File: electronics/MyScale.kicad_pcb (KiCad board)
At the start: 4 copper layers, 80 x 60.1 mm, 101 parts, among them J1 Conn_01x03, J10 Conn_02x03_Odd_Even, J2 Conn_01x03, J3 Conn_01x03, J4 Conn_01x03, J5 Conn_01x02_MountingPin, J6 12402012E212A, J7 SIM_Card, J8 Conn_01x02_MountingPin, J9 Conn_Coaxial_Small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

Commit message: electronics: add 3D models
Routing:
- net GND: vias 116 -> 135
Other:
- board size 80 x 60.1 mm -> 80 x 60 mm
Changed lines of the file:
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@@
 		(sheetname "/Charger/")
 		(sheetfile "charger.kicad_sch")
-		(units
-			(unit
-				(name "A")
-				(pins "1" "6" "16" "2" "4" "9" "11" "12" "17" "8" "5" "13" "14" "15"
-					"10" "3" "7"
-				)
-			)
-		)
 		(attr smd)
 		(duplicate_pad_numbers_are_jumpers no)
@@
 		)
 		(embedded_fonts no)
-		(model "../nRobotics.3dshapes/TI_RTE0016C.stp"
+		(model "${KIPRJMOD}/MyScale.3dshapes/TI_RTE0016C.stp"
 			(offset
 				(xyz 0 0 0)
@@
 		(sheetname "/Radio/")
 		(sheetfile "radio.kicad_sch")
-		(units
-			(unit
-				(name "A")
-				(pins "1" "2" "4" "6" "3" "11" "5" "9" "10" "7" "8")
-			)
-		)
 		(attr smd)
 		(duplicate_pad_numbers_are_jumpers no)
@@
 		)
 		(embedded_fonts no)
-		(model "${KIPRJMOD}/portsupply.3dshapes/TI_DQC0010A.stp"
+		(model "${KIPRJMOD}/MyScale.3dshapes/TI_DQC0010A.stp"
 			(offset
 				(xyz 0 0 0)
@@
 	)
 	(gr_line
-		(start 65 114.905)
+		(start 65 115)
 		(end 145 115)
 		(stroke
@@
 	(gr_line
 		(start 65 175)
-		(end 65 114.905)
+		(end 65 115)
 		(stroke
 			(width 0.05)
@@
 	)
 	(via
+		(at 126.3 142.65)
+		(size 0.45)
+		(drill 0.25)
+		(layers "F.Cu" "B.Cu")
+		(free yes)
+		(net "GND")
+	)
+	(via
+		(at 138.7 126.95)
+		(size 0.6)
+		(drill 0.3)
+		(layers "F.Cu" "B.Cu")
+		(free yes)
+		(net "GND")
+	)
+	(via
 		(at 106.45 134.7)
 		(size 0.45)
@@
 	)
 	(via
+		(at 103.15 151.75)
+		(size 0.6)
+		(drill 0.3)
+		(layers "F.Cu" "B.Cu")
+		(free yes)
+		(net "GND")
+	)
+	(via
 		(at 103.75 122.7)
 		(size 0.6)
@@
 	)
 	(via
+		(at 139.75 128.15)
+		(size 0.6)
+		(drill 0.3)
+		(layers "F.Cu" "B.Cu")
+		(free yes)
+		(net "GND")
+	)
+	(via
 		(at 111.2 148.55)
 		(size 0.6)
@@
 	)
 	(via
+		(at 134.75 128.15)
+		(size 0.6)
+		(drill 0.3)
+		(layers "F.Cu" "B.Cu")
+		(free yes)
+		(net "GND")
+	)
+	(via
 		(at 86.45 131.85)
 		(size 0.6)
@@
 	)
 	(via
-		(at 126.5 142.15)
+		(at 126.2 141.85)
 		(size 0.45)
 		(drill 0.25)
@@
 	)
 	(via
+		(at 74.5 143.05)
+		(size 0.45)
+		(drill 0.25)
+		(layers "F.Cu" "B.Cu")
+		(free yes)
+		(net "GND")
+	)
+	(via
 		(at 142.8 160.4)
 		(size 0.6)
@@
 	)
 	(via
+		(at 123.25 141.25)
+		(size 0.6)
+		(drill 0.3)
+		(layers "F.Cu" "B.Cu")
+		(free yes)
+		(net "GND")
+	)
+	(via
 		(at 102 125)
 		(size 0.6)
@@
 	)
 	(via
+		(at 137.1 146.85)
+		(size 0.6)
+		(drill 0.3)
+		(layers "F.Cu" "B.Cu")
+		(free yes)
+		(net "GND")
+	)
+	(via
 		(at 96.6 173.25)
 		(size 0.6)
@@
 	)
 	(via
+		(at 135.5 126.85)
+		(size 0.6)
+		(drill 0.3)
+		(layers "F.Cu" "B.Cu")
+		(free yes)
+		(net "GND")
+	)
+	(via
 		(at 112.7 151.7)
 		(size 0.6)
@@
 	)
 	(via
+		(at 137.15 126.95)
+		(size 0.6)
+		(drill 0.3)
+		(layers "F.Cu" "B.Cu")
+		(free yes)
+		(net "GND")
+	)
+	(via
+		(at 101.95 156.3)
+		(size 0.6)
+		(drill 0.3)
+		(layers "F.Cu" "B.Cu")
+		(free yes)
+		(net "GND")
+	)
+	(via
 		(at 90.4 147.1)
 		(size 0.6)
@@
 	)
 	(via
+		(at 104.45 150.4)
+		(size 0.6)
+		(drill 0.3)
+		(layers "F.Cu" "B.Cu")
+		(free yes)
+		(net "GND")
+	)
+	(via
 		(at 92.3 135.35)
 		(size 0.6)
@@
 	)
 	(via
+		(at 70.3 129.65)
+		(size 0.6)
+		(drill 0.3)
+		(layers "F.Cu" "B.Cu")
+		(free yes)
+		(net "GND")
+	)
+	(via
 		(at 103.85 136.45)
 		(size 0.45)
@@
 	)
 	(via
+		(at 135.35 146.35)
+		(size 0.6)
+		(drill 0.3)
+		(layers "F.Cu" "B.Cu")
+		(free yes)
+		(net "GND")
+	)
+	(via
 		(at 112.1 133.8)
 		(size 0.45)
@@
 	)
 	(via
+		(at 74.45 145.25)
+		(size 0.45)
+		(drill 0.25)
+		(layers "F.Cu" "B.Cu")
+		(free yes)
+		(net "GND")
+	)
+	(via
+		(at 134.1 143.6)
+		(size 0.6)
+		(drill 0.3)
+		(layers "F.Cu" "B.Cu")
+		(free yes)
+		(net "GND")
+	)
+	(via
 		(at 78.25 132.45)
 		(size 0.6)
@@
 	)
 	(via
+		(at 108.5 155.95)
+		(size 0.6)
+		(drill 0.3)
+		(layers "F.Cu" "B.Cu")
+		(free yes)
+		(net "GND")
+	)
+	(via
 		(at 106.85 116.65)
 		(size 0.6)
@@
 	)
 	(via
+		(at 68.85 128.5)
+		(size 0.6)
+		(drill 0.3)
+		(layers "F.Cu" "B.Cu")
+		(free yes)
+		(net "GND")
+	)
+	(via
 		(at 113 146.15)
 		(size 0.45)
@@
 	)
 	(via
+		(at 116.4 164.8)
+		(size 0.6)
+		(drill 0.3)
+		(layers "F.Cu" "B.Cu")
+		(free yes)
+		(net "GND")
+	)
+	(via
 		(at 92.05 142.55)
 		(size 0.6)
@@
 		(polygon
 			(pts
-				(xy 65.05 115) (xy 145 115) (xy 145.05 175.1) (xy 65.05 175.1)
+				(xy 65 115) (xy 145 115) (xy 145 175) (xy 65 175)
 			)
 		)

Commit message: electronics: final touches
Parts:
- removed C3, C7: C, Capacitor_SMD:C_0402_1005Metric
- removed R15: 0R, Resistor_SMD:R_0402_1005Metric
- added Q2: Q_NMOS_GSD, Package_TO_SOT_SMD:SOT-23-3, F.Cu at (107.5, 130.7)
- added R30: 10k, Resistor_SMD:R_0603_1608Metric, F.Cu at (107.5, 127.9)
- added R31: 0R, Resistor_SMD:R_0603_1608Metric, F.Cu at (74.5, 152.2)
- added REF**: Tab, MyScale:KikitTab, F.Cu at (105.6, 114.3)
- added REF**: Tab, MyScale:KikitTab, F.Cu at (110.4, 175.6)
- added REF**: Tab, MyScale:KikitTab, F.Cu at (64.1, 145.9)
- added REF**: Tab, MyScale:KikitTab, F.Cu at (145.7, 147.8)
- added TP1: TestPoint, TestPoint:TestPoint_Pad_D1.0mm, B.Cu at (75.6, 134.2)
- added TP2: TestPoint, TestPoint:TestPoint_Pad_D1.0mm, B.Cu at (85.3, 154.4)
- added TP3: TestPoint, TestPoint:TestPoint_Pad_D1.0mm, B.Cu at (111.3, 146.0)
- added TP4: TestPoint, TestPoint:TestPoint_Pad_D1.0mm, B.Cu at (104.8, 142.9)
- U3: value ~ -> TXU0202
- moved J9 3.82 mm to (88.3, 122.4)
- moved D2 2.40 mm to (104.0, 132.2)
- moved R11 2.40 mm to (104.2, 129.1)
- moved R12 2.40 mm to (104.2, 130.6)
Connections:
- J7 pad CD: (no net) -> /Radio/SimDet
- J7 pad SH: (no net) -> GND
- J9 pad 1: Net-(J9-In) -> /Radio/RfAnt
- R12 pad 2: GND -> Net-(Q2-D)
- U3 pad 1: Net-(U1-PD_SCK) -> Net-(U1-DOUT)
- U3 pad 4: /Sck -> /Dout
- U3 pad 5: /Dout -> /Sck
- U3 pad 8: Net-(U1-DOUT) -> Net-(U1-PD_SCK)
- U4 pad 23: unconnected-(U4-UART_LOG_TXD-Pad23) -> Net-(U4-UART_LOG_TXD)
- U4 pad 34: unconnected-(U4-USIM_DET-Pad34) -> Net-(U4-USIM_DET)
- U4 pad 6: unconnected-(U4-USB_BOOT-Pad6) -> Net-(U4-USB_BOOT)
- U4 pad 98: unconnected-(U4-GNSS_PWRCTL-Pad98) -> GND
- U5 pad 25: /Dout -> /Sck
- U5 pad 26: /Sck -> /Dout
- U5 pad 46: unconnected-(U5-PB9-Pad46) -> /BatSenseEnable
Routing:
- net Net-(U4-USIM_DET): track 0.00 -> 24.5 mm, vias 0 -> 2
- net /BatSenseEnable: track 0.00 -> 9.36 mm
- net Net-(U4-USB_BOOT): track 0.00 -> 3.97 mm, vias 0 -> 1
- net Net-(Q2-D): track 0.00 -> 3.04 mm
- net Net-(U4-UART_LOG_TXD): track 0.00 -> 2.95 mm, vias 0 -> 1
- net Net-(J9-In): track 2.69 -> 0.00 mm
- net /VbatSense: track 14.6 -> 16.8 mm
- net /RadioUartTx: track 40.2 -> 42.3 mm
- net +1V8: track 21.3 -> 23.3 mm
- net /Radio/SimDet: track 0.00 -> 1.94 mm
- net VBAT: track 90.0 -> 91.7 mm
- net Net-(U1-PD_SCK): track 3.49 -> 4.64 mm
- net /RadioUartRx: track 42.3 -> 43.3 mm
- net Net-(U1-DOUT): track 3.54 -> 4.49 mm, vias 0 -> 2
- net GND: vias 135 -> 143

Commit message: electronics: add MPNs
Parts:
- R17: value 24k -> 20k
- R8: value 100k -> 20k

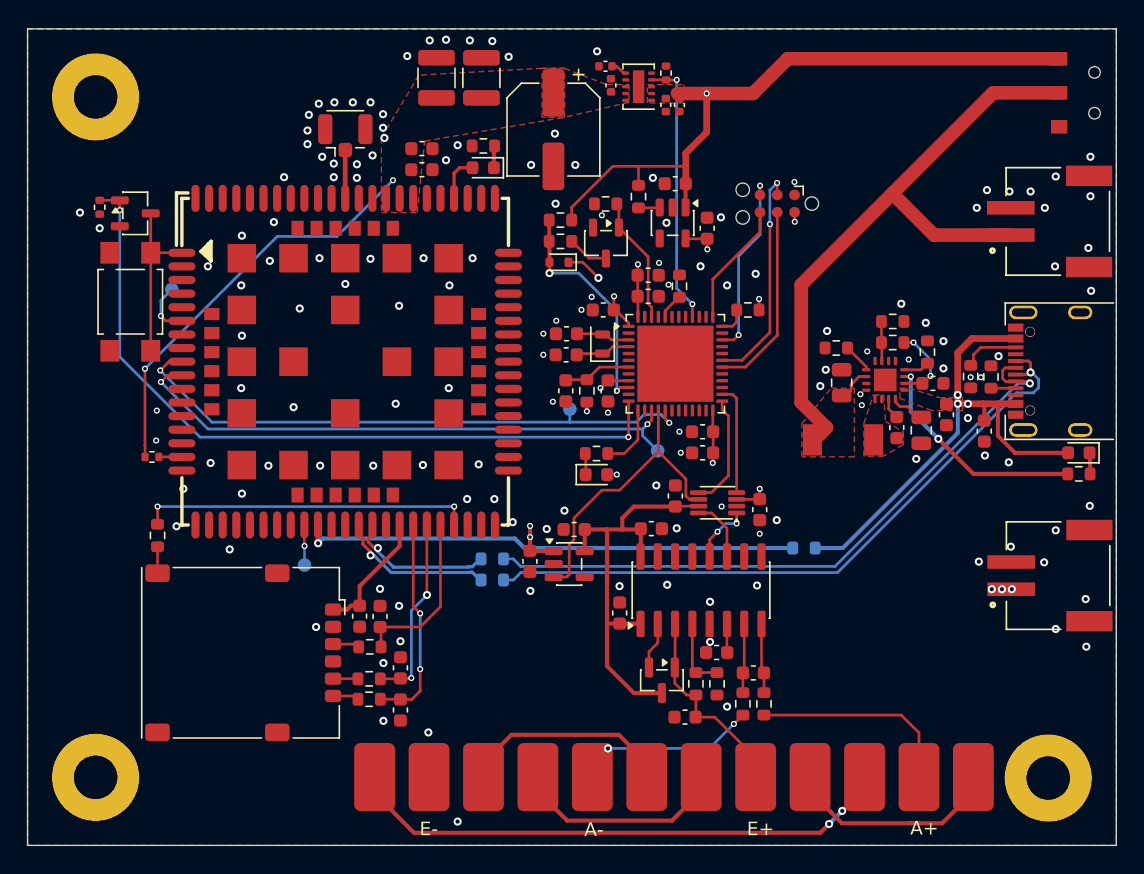
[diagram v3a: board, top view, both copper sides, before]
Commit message: electronics: simplify BOM and fix issues
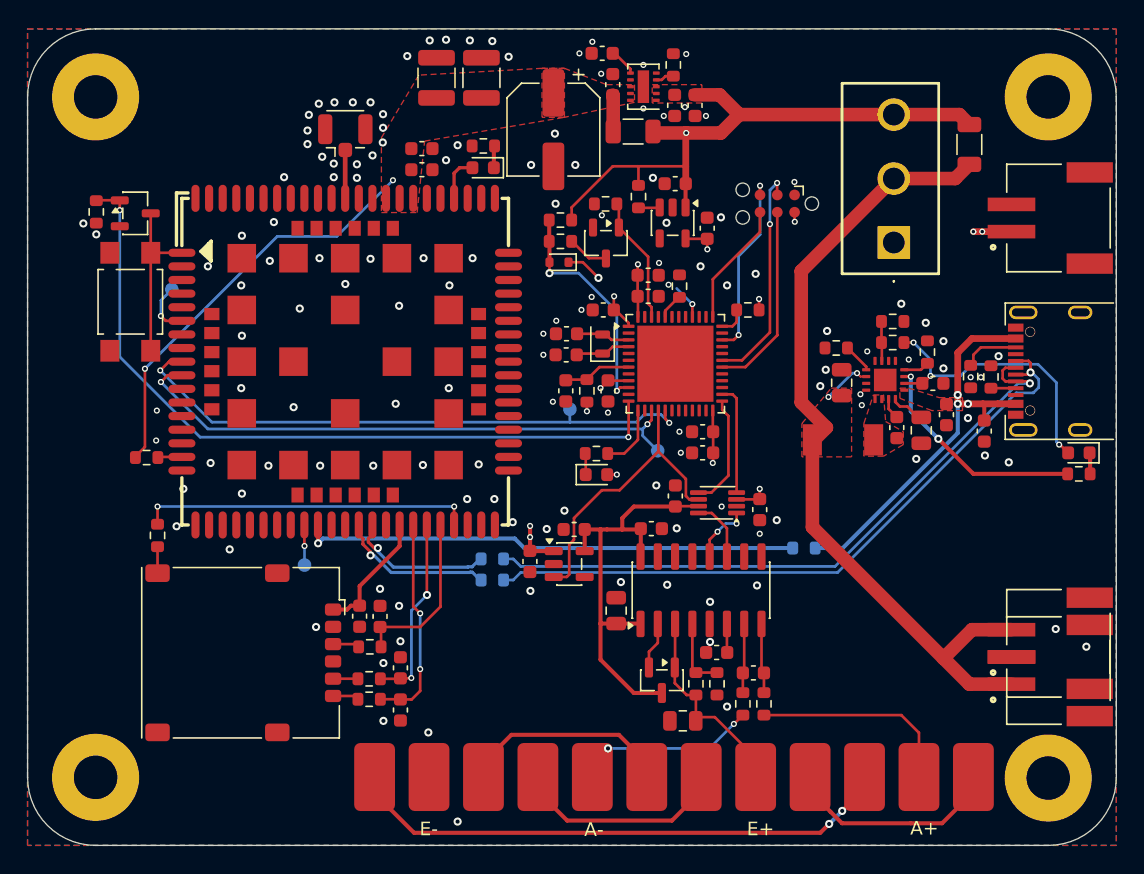
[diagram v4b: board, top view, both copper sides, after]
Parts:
- removed REF** (x4): Tab, MyScale:KikitTab
- added H4: MountingHole_Pad, MountingHole:MountingHole_3.2mm_M3_Pad, F.Cu at (140.0, 120.0)
- added J11: Conn_01x02_MountingPin, MyScale:JST_S2B-PH-SM4-TB(LF)(SN), F.Cu at (140.7, 160.2)
- added R15: 0R, Resistor_SMD:R_1206_3216Metric, F.Cu at (109.5, 122.5)
- added R32: 0R, Resistor_SMD:R_1206_3216Metric, F.Cu at (134.2, 123.5)
- C13, C15: footprint Capacitor_SMD:C_0603_1608Metric -> Capacitor_SMD:C_0805_2012Metric
- C24: value 10p -> 6.8p
- C27, C28, C29, C30: footprint Capacitor_SMD:C_0402_1005Metric -> Capacitor_SMD:C_0603_1608Metric
- C8: value 33p -> 22p
- Q1, Q2: value Q_NMOS_GSD -> SI2302CDS
- R1: value 390R -> 22R
- R10: value 390R -> 5.1k
- R16: value 51R -> 22R
- R17: value 20k -> 10k; footprint Resistor_SMD:R_0402_1005Metric -> Resistor_SMD:R_0603_1608Metric
- R22, R26: footprint Resistor_SMD:R_0402_1005Metric -> Resistor_SMD:R_0603_1608Metric
- SW3: footprint MyScale:CAK_AYZ0102AURLC -> MyScale:NKK_CS12ANW03
- moved J5 33.0 mm to (140.7, 162.2)
- moved J8 26.3 mm to (140.7, 128.9)
- moved SW3 18.4 mm to (128.7, 130.7), turned to 0 degrees
- moved C29 1.15 mm to (114.0, 120.6)
- moved C28 0.98 mm to (107.2, 116.8)
- moved R17 0.80 mm to (112.5, 117.7)
- moved C27 0.65 mm to (112.5, 120.6)
- moved R22 0.43 mm to (70.0, 128.4)
- moved R26 0.39 mm to (73.8, 146.5)
- moved U2 0.35 mm to (110.2, 119.2)
- moved C15 0.32 mm to (113.2, 165.8)
- moved C13 0.31 mm to (108.2, 157.8)
- moved C30 0.14 mm to (108.0, 119.1)
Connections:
- D4 pad 2: VBUS -> /Charger/REGN
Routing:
- net /RadioEnable: track 19.8 -> 3.93 mm, vias 2 -> 1
- net /Charger/REGN: track 5.83 -> 21.5 mm, vias 2 -> 3
- net /Charger/Vpack: track 49.2 -> 64.6 mm, vias 0 -> 2
- net VBUS: track 56.1 -> 48.0 mm, vias 6 -> 5
- net VBAT: track 91.7 -> 84.2 mm
- net /Radio/VbatModule: track 30.4 -> 33.5 mm
- net Net-(U2-CT): track 1.21 -> 2.08 mm
- net GND: vias 143 -> 134
- added copper zone on In2.Cu, net GND
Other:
- outline, holes or cut-outs redrawn
- board text added: "DCEIQ r3"
- board text removed: "DCEIQ r2"

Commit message: electronics: improve deistribution
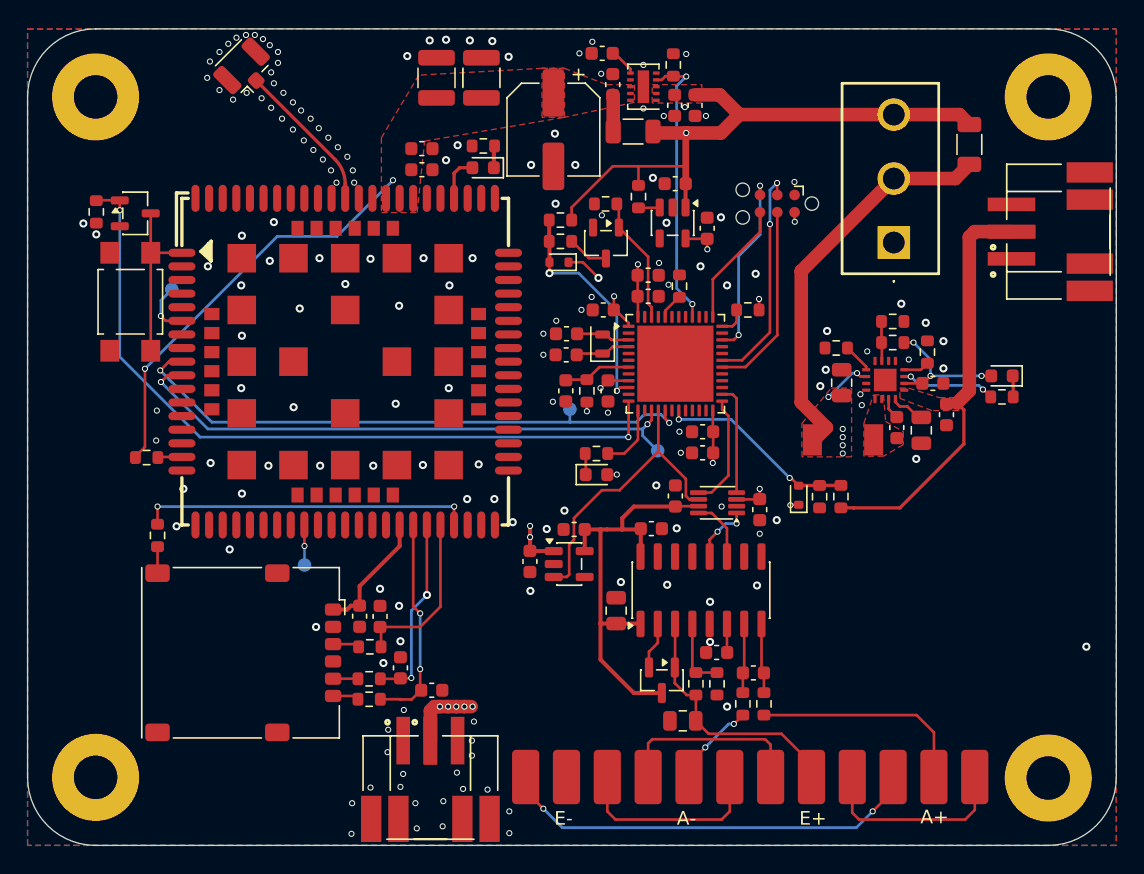
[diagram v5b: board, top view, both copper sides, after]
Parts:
- removed C31: 1u, Capacitor_SMD:C_0603_1608Metric
- removed J6: 12402012E212A, MyScale:AMPH_12402012E212A
- removed R29: 0R, Resistor_SMD:R_0603_1608Metric
- removed R3, R4: 5.1k, Resistor_SMD:R_0603_1608Metric
- added D3: D_Schottky, Diode_SMD:D_SOD-523, F.Cu at (121.7, 149.3)
- added J12: Conn_01x02_MountingPin, MyScale:JST_S2B-PH-SM4-TB(LF)(SN), F.Cu at (140.7, 130.9)
- R27: value 27R -> 20k; moved to F.Cu
- R28: value 27R -> 10k; moved to F.Cu
- moved J11 48.3 mm to (93.6, 170.7), turned to 0 degrees
- moved J5 45.9 mm to (95.6, 170.7), turned to 0 degrees
- moved R27 26.0 mm to (124.8, 149.4), turned to 90 degrees
- moved R28 24.8 mm to (123.2, 149.4), turned to -90 degrees
- moved J1 11.1 mm to (101.6, 170.0)
- moved J9 8.94 mm to (80.7, 117.7), turned to 135 degrees
- moved J2 8.10 mm to (110.6, 170.0)
- moved D4 7.99 mm to (136.6, 140.5)
- moved R10 7.99 mm to (136.6, 142.0)
- moved J3 5.10 mm to (119.6, 170.0)
- moved C22 2.72 mm to (94.7, 163.6), turned to 0 degrees
- moved J4 2.10 mm to (128.6, 170.0)
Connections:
- R27 pad 1: /USBD- -> VBUS
- R27 pad 2: /USBCD- -> /VbusSense
- R28 pad 1: /USBD+ -> /VbusSense
- R28 pad 2: /USBCD+ -> GND
- U4 pad 24: Net-(U4-VBUS) -> unconnected-(U4-VBUS-Pad24)
- U5 pad 19: unconnected-(U5-PB1-Pad19) -> /VbusSense
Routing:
- net /USBCD+: track 49.6 -> 0.00 mm, vias 1 -> 0
- net /USBCD-: track 48.3 -> 0.00 mm, vias 1 -> 0
- net Net-(U4-VBUS): track 36.7 -> 0.00 mm, vias 1 -> 0
- net VBUS: track 48.0 -> 30.0 mm, vias 5 -> 0
- net /RadioEnable: track 3.93 -> 20.8 mm, vias 1 -> 2
- net /Charger/Vpack: track 64.6 -> 80.3 mm, vias 2 -> 11
- net /VbusSense: track 0.00 -> 14.6 mm, vias 0 -> 2
- net /USBD+: track 11.5 -> 0.00 mm, vias 1 -> 0
- net /Charger/REGN: track 21.5 -> 10.3 mm
- net /USBD-: track 10.8 -> 0.00 mm, vias 1 -> 0
- net Net-(U8-STAT): track 16.5 -> 6.97 mm
- net Net-(J1-Pin_1): track 38.7 -> 30.2 mm
- net /Radio/RfAnt: track 3.59 -> 11.2 mm
- net /Load Cell Interface/A-: track 10.9 -> 6.42 mm
- net Net-(J6-CC2): track 4.11 -> 0.00 mm
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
